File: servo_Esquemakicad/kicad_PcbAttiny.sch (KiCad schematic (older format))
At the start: 52 parts, among them J1 Conn_02x02_Odd_Even, J10 Conn_01x04, J11 Conn_01x04, J12 Conn_01x04, J13 Conn_01x04, J4 RF, J5 ESP01, J6 Conn_01x04, J7 Conn_01x04, J8 Conn_01x04, J9 Conn_01x04, K1 SANYOU_SRD_Form_C, K2 SANYOU_SRD_Form_C, K3 SANYOU_SRD_Form_C, K4 SANYOU_SRD_Form_C, K5 SANYOU_SRD_Form_C, K6 SANYOU_SRD_Form_C, K7 SANYOU_SRD_Form_C, K8 SANYOU_SRD_Form_C, Q1 2N2219, Q2 2N2219, Q3 2N2219, Q4 2N2219, Q5 2N2219, Q6 2N2219, Q7 2N2219, Q8 2N2219, U1 ATtiny85V-10PU, U2 74HC595, U5 LM317

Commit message: att
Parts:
- U1: symbol kicad_Poolcontroller-rescue:ATtiny85V-10PU-MCU_Microchip_ATtiny-Pool_Controller-rescue -> kicad_PcbAttiny-rescue:ATtiny85V-10PU-MCU_Microchip_ATtiny-Pool_Controller-rescue-kicad_Poolcontroller-rescue
- gave numbers to parts that had none: 3
- renumbered C4 to C1, D5 to D1, D1 to D2, D6 to D3, D2 to D4, D7 to D5, D3 to D6, D8 to D7, D4 to D8, J13 to J10, J6 to J11, J4 to J2, J5 to J3, J10 to J4, J9 to J5, J11 to J6, J8 to J7, J12 to J8, J7 to J9, K5 to K1, K1 to K2, K6 to K3, K2 to K4, K7 to K5, K3 to K6, K8 to K7, K4 to K8, Q5 to Q2, Q2 to Q3, Q6 to Q4, Q3 to Q5, Q7 to Q6, Q4 to Q7, R9 to R1, R3 to R10, R2 to R11, R1 to R12, R10 to R2, R8 to R5, R7 to R6, R6 to R7, R5 to R8, R4 to R9, U5 to U2, U2 to U3

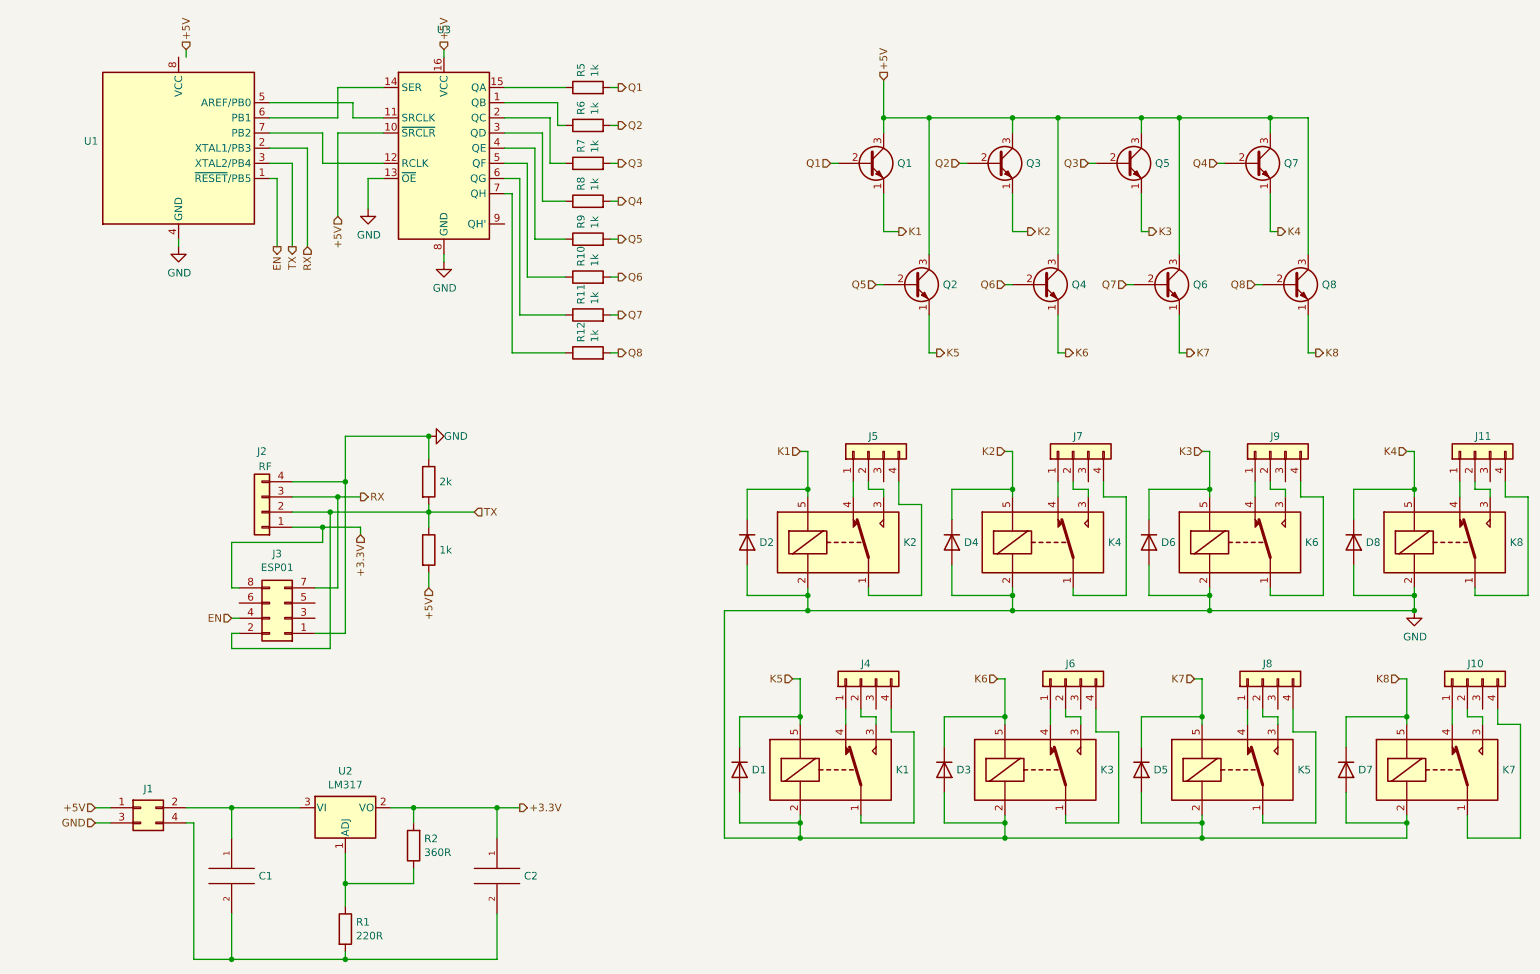
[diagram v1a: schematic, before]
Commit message: retirada de componentes desnecessarios
após analise vi q vários componentes n tinham razão pra existir então foram retirado
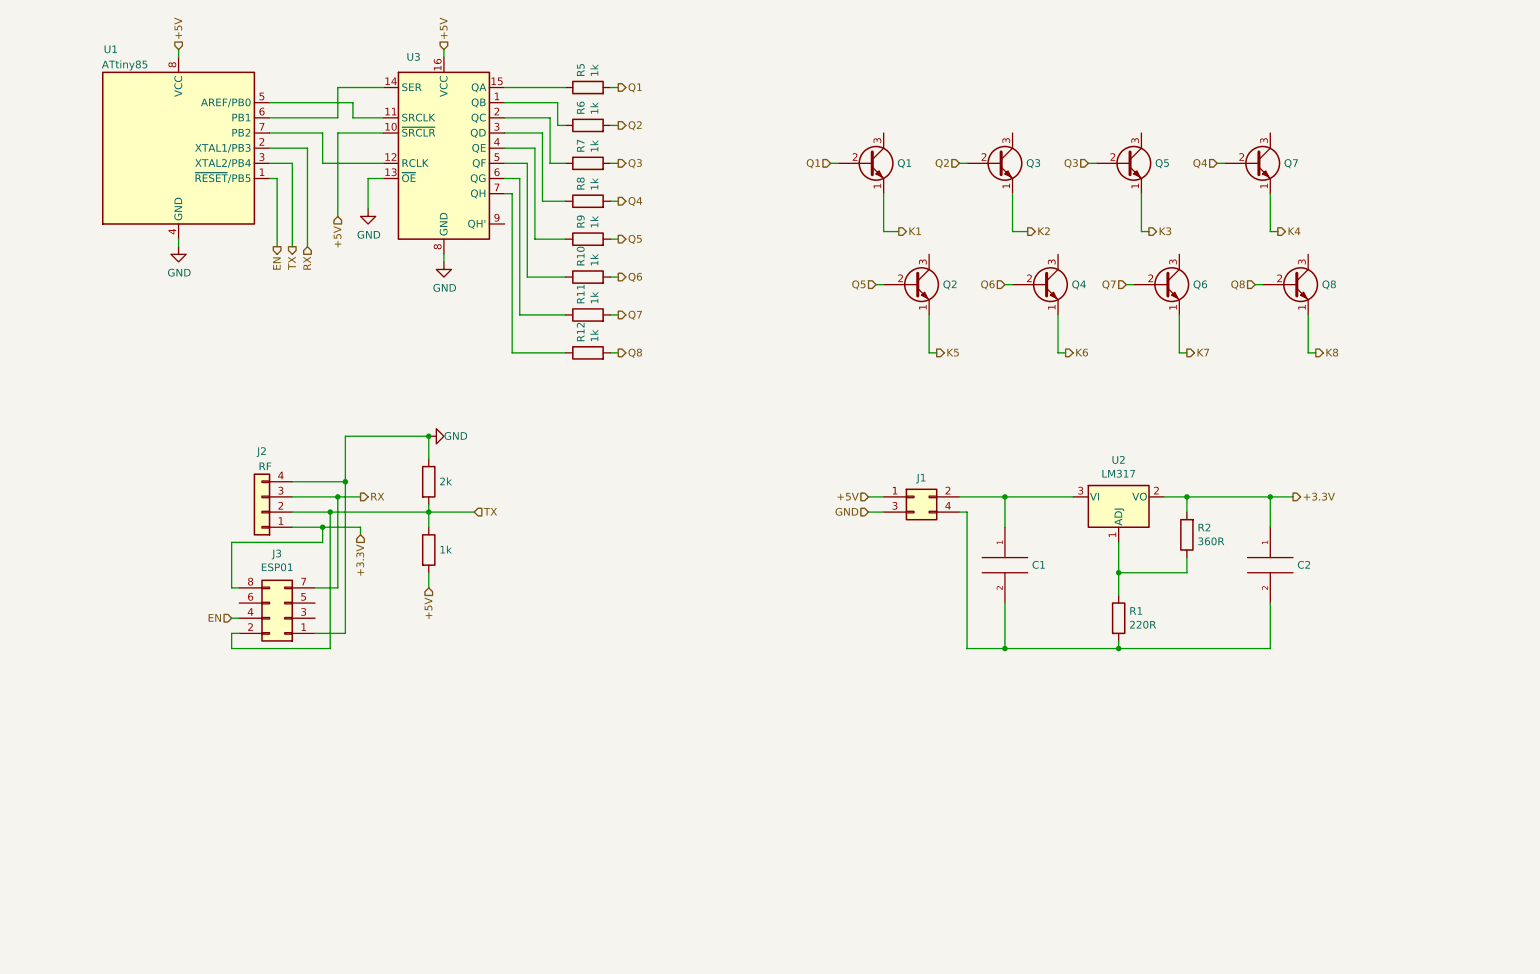
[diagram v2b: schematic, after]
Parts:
- removed D1, D2, D3, D4, D5, D6, D7, D8: 1N4007, Diode_THT:D_DO-41_SOD81_P10.16mm_Horizontal, symbol Diode:1N4007
- removed J10, J11, J4, J5, J6, J7, J8, J9: Conn_01x04, TerminalBlock:TerminalBlock_bornier-4_P5.08mm, symbol Connector_Generic:Conn_01x04
- removed K1, K2, K3, K4, K5, K6, K7, K8: SANYOU_SRD_Form_C, Relay_THT:Relay_SPDT_SANYOU_SRD_Series_Form_C, symbol Relay:SANYOU_SRD_Form_C
- removed U1: ATtiny85V-10PU, Package_DIP:DIP-8_W7.62mm_Socket, symbol kicad_PcbAttiny-rescue:ATtiny85V-10PU-MCU_Microchip_ATtiny-Pool_Controller-resc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
- added U1: ATtiny85, Package_SO:SOIJ-8_5.3x5.3mm_P1.27mm, symbol MCU_Microchip_ATtiny:ATtiny85-20SU
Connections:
- net +5V: now also U1.8 (VCC); no longer Q1.3 (C), Q2.3 (C), Q3.3 (C), Q4.3 (C), Q5.3 (C), Q6.3 (C), Q7.3 (C), Q8.3 (C)
- net EN: now also U1.1 (~RESET~/PB5)
- net GND: now also U1.4 (GND)
- net RX: now also U1.2 (XTAL1/PB3)
- net TX: now also U1.3 (XTAL2/PB4)
- net at U3.11 (SRCLK): now also U1.5 (AREF/PB0)
- net at U3.12 (RCLK): now also U1.7 (PB2)
- net at U3.14 (SER): now also U1.6 (PB1)
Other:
- moved on the sheet: C1, C2, J1, R1, R2, U2

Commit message: atualizações do esquematico e design PCB
Atualizada o esquemático com as novas conexões p/ os transistores
Atualizado o designe PCB com os novos footprints
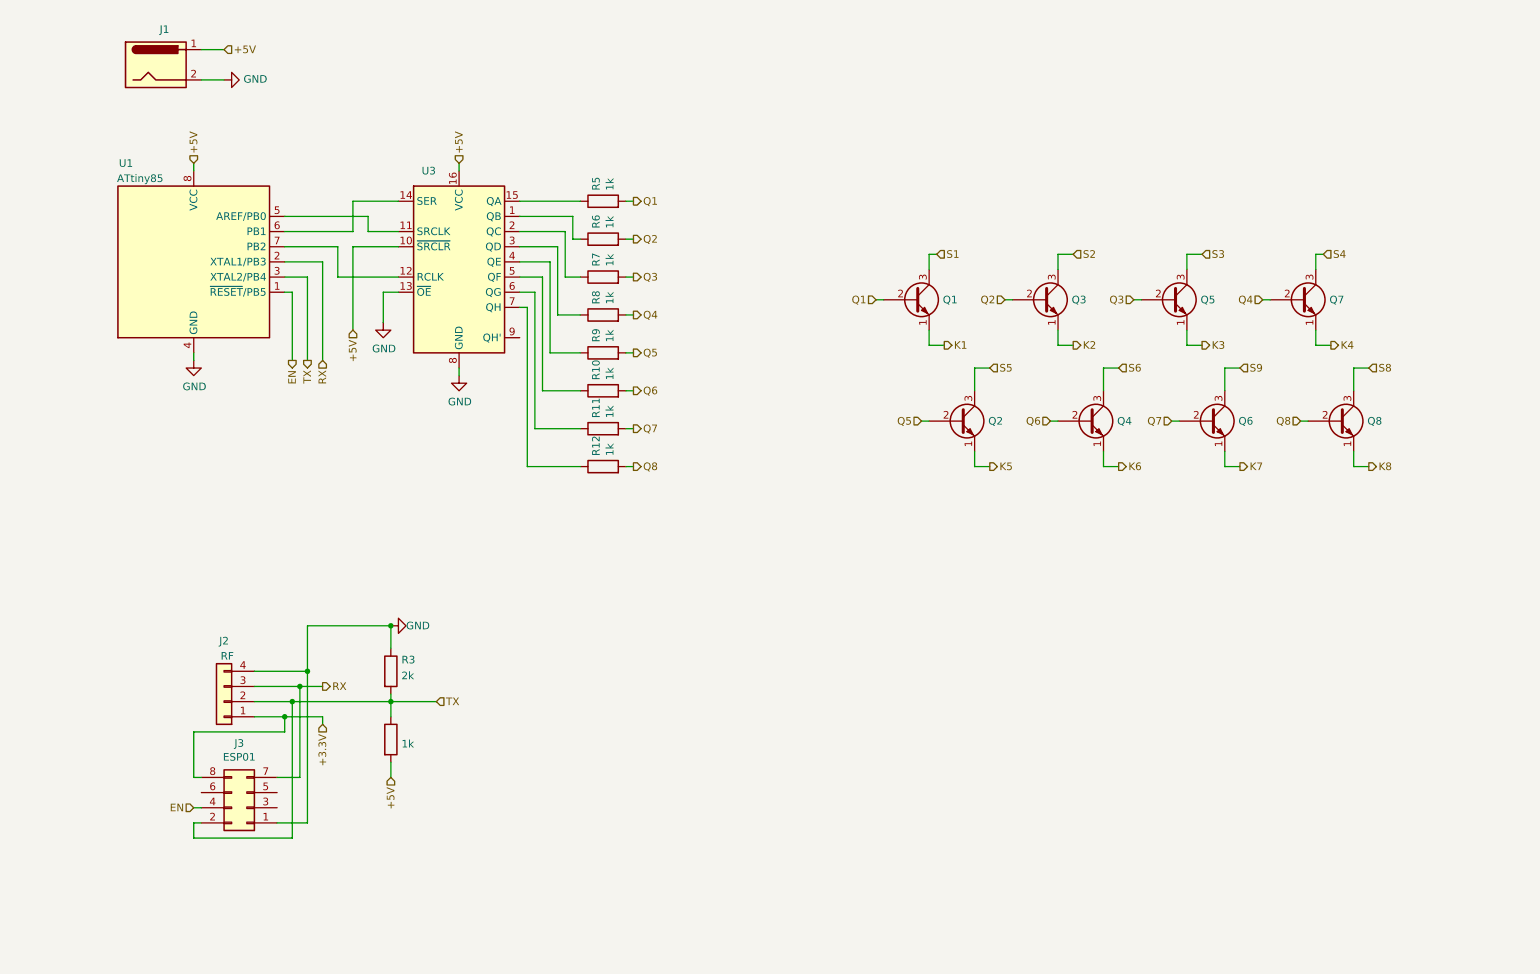
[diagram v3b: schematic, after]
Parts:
- removed C1: 0.1u, Capacitor_THT:CP_Radial_D5.0mm_P2.50mm, symbol pspice:C
- removed C2: 10u, Capacitor_THT:CP_Radial_D5.0mm_P2.50mm, symbol pspice:C
- removed J1: Conn_02x02_Odd_Even, symbol Connector_Generic:Conn_02x02_Odd_Even
- removed R1: 220R, Resistor_THT:R_Axial_DIN0207_L6.3mm_D2.5mm_P10.16mm_Horizontal, symbol Device:R
- removed R2: 360R, Resistor_THT:R_Axial_DIN0207_L6.3mm_D2.5mm_P10.16mm_Horizontal, symbol Device:R
- removed U2: LM317, Package_TO_SOT_THT:TO-220-3_Horizontal_TabDown, symbol Regulator_Linear:LM317_3PinPackage
- added J1: Jack-DC, Connector_BarrelJack:BarrelJack_Horizontal, symbol Connector:Jack-DC
- R3, R4: footprint (none) -> Resistor_THT:R_Axial_DIN0207_L6.3mm_D2.5mm_P10.16mm_Horizontal
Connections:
- net +5V: now also J1.1
- net GND: now also J1.2
- net S5: now reaches Q2.3 (C)
- net S6: now reaches Q4.3 (C)
- net S9: now reaches Q6.3 (C)
- net S8: now reaches Q8.3 (C)
- net S1: now reaches Q1.3 (C)
- net S2: now reaches Q3.3 (C)
- net S3: now reaches Q5.3 (C)
- net S4: now reaches Q7.3 (C)
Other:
- moved on the sheet: J2, J3, Q1, Q2, Q3, Q4, Q5, Q6, Q7, Q8, R10, R11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

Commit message: trilhas terminadas
Falta as vias para as saídas dos transistores.
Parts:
- removed U1: ATtiny85, Package_SO:SOIJ-8_5.3x5.3mm_P1.27mm, symbol MCU_Microchip_ATtiny:ATtiny85-20SU
- added U4: ATtiny85-20PU, Package_DIP:DIP-8_W7.62mm, symbol MCU_Microchip_ATtiny:ATtiny85-20PU
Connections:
- net +3.3V is gone; now on net +5V: J2.1 (Pin_1), J3.8 (Pin_8)
- net +5V: now also U4.8 (VCC)
- net EN: now also U4.1 (~RESET~/PB5)
- net GND: now also U4.4 (GND)
- net RX: now also U4.2 (XTAL1/PB3)
- net TX: now also U4.3 (XTAL2/PB4)
- net at U3.11 (SRCLK): now also U4.5 (AREF/PB0)
- net at U3.12 (RCLK): now also U4.7 (PB2)
- net at U3.14 (SER): now also U4.6 (PB1)
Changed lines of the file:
@@
 	1900 6050 1950 6050
 Text HLabel 2750 5400 3    50   Input ~ 0
-+3.3V
++5V
 $Comp
 L Connector_Generic:Conn_01x04 J2
@@
 Wire Wire Line
 	3200 5750 3200 5650
-$Comp
-L MCU_Microchip_ATtiny:ATtiny85-20SU U1
-U 1 1 610A19D1
-P 1900 2350
-F 0 "U1" H 1500 3000 50  0000 R CNN
-F 1 "ATtiny85" H 1700 2900 50  0000 R CNN
-F 2 "Package_SO:SOIJ-8_5.3x5.3mm_P1.27mm" H 1900 2350 50  0001 C CIN
-F 3 "http://ww1.microchip.com/downloads/en/DeviceDoc/atmel-2586-avr-8-bit-microcontroller-attiny25-attiny45-attiny85_datasheet.pdf" H 1900 2350 50  0001 C CNN
-	1    1900 2350
-	1    0    0    -1
-$EndComp
 Wire Wire Line
 	1900 1700 1900 1750
@@
 Wire Wire Line
 	1950 1150 2100 1150
+$Comp
+L MCU_Microchip_ATtiny:ATtiny85-20PU U4
+U 1 1 6108C5C1
+P 1900 2350
+F 0 "U4" H 1371 2396 50  0000 R CNN
+F 1 "ATtiny85-20PU" H 1371 2305 50  0000 R CNN
+F 2 "Package_DIP:DIP-8_W7.62mm" H 1900 2350 50  0001 C CIN
+F 3 "http://ww1.microchip.com/downloads/en/DeviceDoc/atmel-2586-avr-8-bit-microcontroller-attiny25-attiny45-attiny85_datasheet.pdf" H 1900 2350 50  0001 C CNN
+	1    1900 2350
+	1    0    0    -1
+$EndComp
 $EndSCHEMATC
